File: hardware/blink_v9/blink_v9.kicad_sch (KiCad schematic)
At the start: 117 parts, among them J1 Conn_01x02, J14 Conn_02x16_Odd_Even, J15 Conn_01x01, J16 Conn_01x01, J5 Conn_01x06_Pin, J7 Conn_01x06_Pin, J8 Conn_01x06, J9 USB_C_Receptacle, Q1 S8550, Q2 S8050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

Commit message: start swap usb rx/tx
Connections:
- net LEDMY: now also U4.59 (PB7); no longer U4.43 (PA10)
- net NCOL1: now also U4.58 (PB6); no longer U4.42 (PA9)
- net USB_RX: now also U4.42 (PA9); no longer U4.58 (PB6)
- net USB_TX: now also U4.43 (PA10); no longer U4.59 (PB7)
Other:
- moved on the sheet: R17, R20
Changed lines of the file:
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@@
     (stroke (width 0) (type default))
   )
-  (wire (pts (xy 278.13 55.88) (xy 278.13 59.69))
+  (wire (pts (xy 283.21 43.18) (xy 283.21 46.99))
     (stroke (width 0) (type default))
   )
@@
     (stroke (width 0) (type default))
   )
-  (wire (pts (xy 261.62 55.88) (xy 261.62 59.69))
+  (wire (pts (xy 266.7 43.18) (xy 266.7 46.99))
     (stroke (width 0) (type default))
   )
@@
     (effects (font (size 1.27 1.27)) (justify left bottom))
   )
+  (label "USB_RX" (at 242.57 55.88 0) (fields_autoplaced)
+    (effects (font (size 1.27 1.27)) (justify left bottom))
+  )
   (label "DB3" (at 207.01 50.8 180) (fields_autoplaced)
     (effects (font (size 1.27 1.27)) (justify right bottom))
@@
     (effects (font (size 1.27 1.27)) (justify right bottom))
   )
-  (label "LEDMY" (at 242.57 58.42 0) (fields_autoplaced)
-    (effects (font (size 1.27 1.27)) (justify left bottom))
-  )
   (label "HSE_IN" (at 207.01 43.18 180) (fields_autoplaced)
     (effects (font (size 1.27 1.27)) (justify right bottom))
@@
     (effects (font (size 1.27 1.27)) (justify right bottom))
   )
+  (label "USB_TX" (at 242.57 58.42 0) (fields_autoplaced)
+    (effects (font (size 1.27 1.27)) (justify left bottom))
+  )
   (label "NROW5" (at 365.76 58.42 0) (fields_autoplaced)
     (effects (font (size 1.27 1.27)) (justify left bottom))
@@
     (effects (font (size 1.27 1.27)) (justify left bottom))
   )
-  (label "USB_TX" (at 242.57 93.98 0) (fields_autoplaced)
-    (effects (font (size 1.27 1.27)) (justify left bottom))
-  )
   (label "NCOL7" (at 365.76 48.26 0) (fields_autoplaced)
     (effects (font (size 1.27 1.27)) (justify left bottom))
@@
     (effects (font (size 1.27 1.27)) (justify left bottom))
   )
-  (label "PPS_OUT" (at 261.62 50.8 0) (fields_autoplaced)
+  (label "PPS_OUT" (at 266.7 38.1 0) (fields_autoplaced)
     (effects (font (size 1.27 1.27)) (justify left bottom))
   )
@@
     (effects (font (size 1.27 1.27)) (justify right bottom))
   )
-  (label "PPS_OUT" (at 278.13 50.8 0) (fields_autoplaced)
+  (label "PPS_OUT" (at 283.21 38.1 0) (fields_autoplaced)
     (effects (font (size 1.27 1.27)) (justify left bottom))
   )
@@
     (effects (font (size 1.27 1.27)) (justify left bottom))
   )
-  (label "MON_PPS" (at 261.62 59.69 0) (fields_autoplaced)
+  (label "MON_PPS" (at 266.7 46.99 0) (fields_autoplaced)
     (effects (font (size 1.27 1.27)) (justify left bottom))
   )
-  (label "AUX_MON_PPS" (at 278.13 59.69 0) (fields_autoplaced)
+  (label "AUX_MON_PPS" (at 283.21 46.99 0) (fields_autoplaced)
     (effects (font (size 1.27 1.27)) (justify left bottom))
   )
@@
     (effects (font (size 1.27 1.27)) (justify left bottom))
   )
-  (label "USB_RX" (at 242.57 91.44 0) (fields_autoplaced)
-    (effects (font (size 1.27 1.27)) (justify left bottom))
-  )
   (label "AUD_IN" (at 207.01 55.88 180) (fields_autoplaced)
     (effects (font (size 1.27 1.27)) (justify right bottom))
@@
     (effects (font (size 1.27 1.27)) (justify left bottom))
   )
-  (label "NCOL1" (at 242.57 55.88 0) (fields_autoplaced)
-    (effects (font (size 1.27 1.27)) (justify left bottom))
-  )
   (label "SWDCLK" (at 120.65 85.09 0) (fields_autoplaced)
     (effects (font (size 1.27 1.27)) (justify left bottom))
@@
     (effects (font (size 1.27 1.27)) (justify left bottom))
   )
+  (label "NCOL1" (at 242.57 91.44 0) (fields_autoplaced)
+    (effects (font (size 1.27 1.27)) (justify left bottom))
+  )
   (label "Left" (at 46.99 182.88 0) (fields_autoplaced)
     (effects (font (size 1.27 1.27)) (justify left bottom))
@@
     (effects (font (size 1.27 1.27)) (justify right bottom))
   )
+  (label "LEDMY" (at 242.57 93.98 0) (fields_autoplaced)
+    (effects (font (size 1.27 1.27)) (justify left bottom))
+  )
   (label "LED6" (at 152.4 137.16 0) (fields_autoplaced)
     (effects (font (size 1.27 1.27)) (justify left bottom))
@@
     )
   )
-  (symbol (lib_id "Device:R_Small_US") (at 278.13 53.34 0) (unit 1)
+  (symbol (lib_id "Device:R_Small_US") (at 283.21 40.64 0) (unit 1)
     (in_bom yes) (on_board yes) (dnp no) (fields_autoplaced)
-    (property "Reference" "R20" (at 280.67 52.07 0)
+    (property "Reference" "R20" (at 285.75 39.37 0)
       (effects (font (size 1.27 1.27)) (justify left))
     )
-    (property "Value" "1K0" (at 280.67 54.61 0)
+    (property "Value" "1K0" (at 285.75 41.91 0)
       (effects (font (size 1.27 1.27)) (justify left))
     )
-    (property "Footprint" "Resistor_SMD:R_0603_1608Metric" (at 278.13 53.34 0)
+    (property "Footprint" "Resistor_SMD:R_0603_1608Metric" (at 283.21 40.64 0)
       (effects (font (size 1.27 1.27)) hide)
     )
-    (property "Datasheet" "https://jlcpcb.com/partdetail/Yageo-AC0805FR0751RL/C144556#:~:text=Datasheet-,Download,-Source" (at 278.13 53.34 0)
+    (property "Datasheet" "https://jlcpcb.com/partdetail/Yageo-AC0805FR0751RL/C144556#:~:text=Datasheet-,Download,-Source" (at 283.21 40.64 0)
       (effects (font (size 1.27 1.27)) hide)
     )
-    (property "LCSC" "" (at 278.13 53.34 0)
+    (property "LCSC" "" (at 283.21 40.64 0)
       (effects (font (size 1.27 1.27)) hide)
     )
-    (property "JLCPCB Part #" "C21190" (at 278.13 53.34 0)
+    (property "JLCPCB Part #" "C21190" (at 283.21 40.64 0)
       (effects (font (size 1.27 1.27)) hide)
     )
@@
     )
   )
-  (symbol (lib_id "Device:R_Small_US") (at 261.62 53.34 0) (unit 1)
+  (symbol (lib_id "Device:R_Small_US") (at 266.7 40.64 0) (unit 1)
     (in_bom yes) (on_board yes) (dnp no) (fields_autoplaced)
-    (property "Reference" "R17" (at 264.16 52.07 0)
+    (property "Reference" "R17" (at 269.24 39.37 0)
       (effects (font (size 1.27 1.27)) (justify left))
     )
-    (property "Value" "1K0" (at 264.16 54.61 0)
+    (property "Value" "1K0" (at 269.24 41.91 0)
       (effects (font (size 1.27 1.27)) (justify left))
     )
-    (property "Footprint" "Resistor_SMD:R_0603_1608Metric" (at 261.62 53.34 0)
+    (property "Footprint" "Resistor_SMD:R_0603_1608Metric" (at 266.7 40.64 0)
       (effects (font (size 1.27 1.27)) hide)
     )
-    (property "Datasheet" "https://jlcpcb.com/partdetail/Yageo-AC0805FR0751RL/C144556#:~:text=Datasheet-,Download,-Source" (at 261.62 53.34 0)
+    (property "Datasheet" "https://jlcpcb.com/partdetail/Yageo-AC0805FR0751RL/C144556#:~:text=Datasheet-,Download,-Source" (at 266.7 40.64 0)
       (effects (font (size 1.27 1.27)) hide)
     )
-    (property "LCSC" "" (at 261.62 53.34 0)
+    (property "LCSC" "" (at 266.7 40.64 0)
       (effects (font (size 1.27 1.27)) hide)
     )
-    (property "JLCPCB Part #" "C21190" (at 261.62 53.34 0)
+    (property "JLCPCB Part #" "C21190" (at 266.7 40.64 0)
       (effects (font (size 1.27 1.27)) hide)
     )

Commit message: rename sync_in2 to aux
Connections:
- net SYNC_IN2 renamed AUX_SYNC_IN
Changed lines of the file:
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@@
     (effects (font (size 1.27 1.27)) (justify left bottom))
   )
-  (label "SYNC_IN2" (at 207.01 71.12 180) (fields_autoplaced)
+  (label "AUX_SYNC_IN" (at 207.01 71.12 180) (fields_autoplaced)
     (effects (font (size 1.27 1.27)) (justify right bottom))
   )
@@
     (effects (font (size 1.27 1.27)) (justify right bottom))
   )
-  (global_label "SYNC_IN2" (shape input) (at 287.02 217.17 0) (fields_autoplaced)
+  (global_label "AUX_SYNC_IN" (shape input) (at 287.02 217.17 0) (fields_autoplaced)
     (effects (font (size 1.27 1.27)) (justify left))
     (property "Intersheetrefs" "${INTERSHEET_REFS}" (at 298.9368 217.17 0)

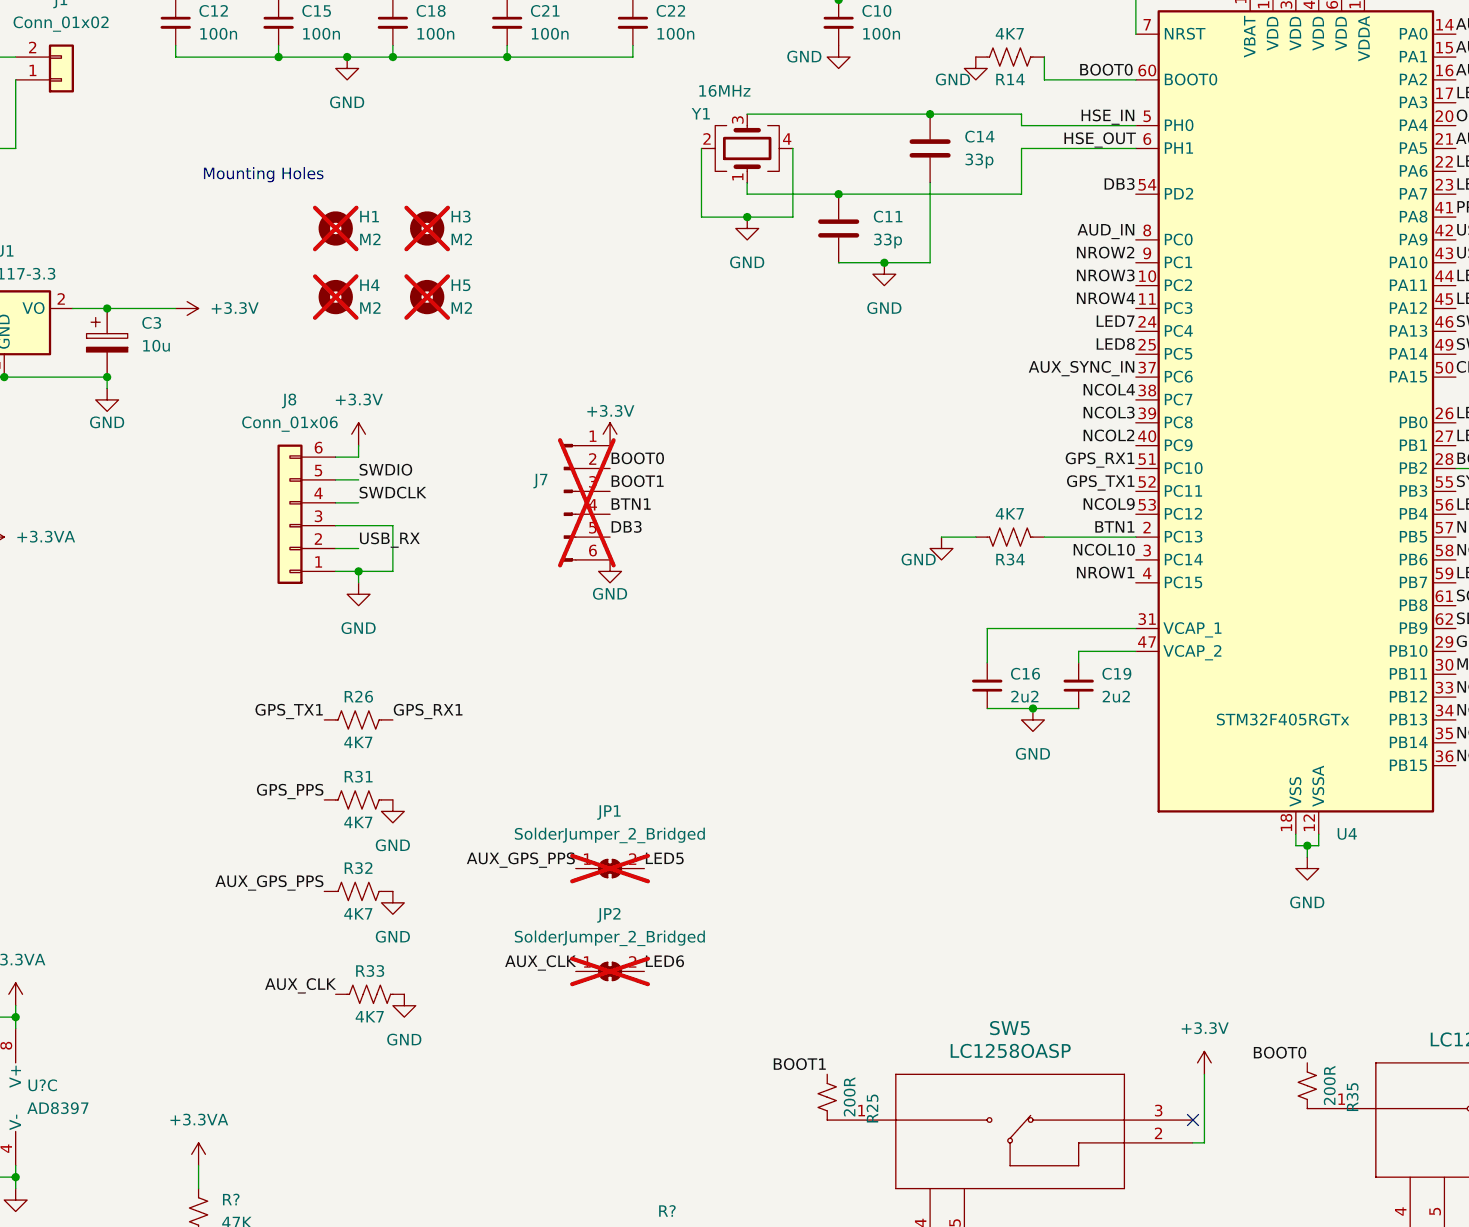
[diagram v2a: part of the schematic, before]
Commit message: update jumpers and swtiches
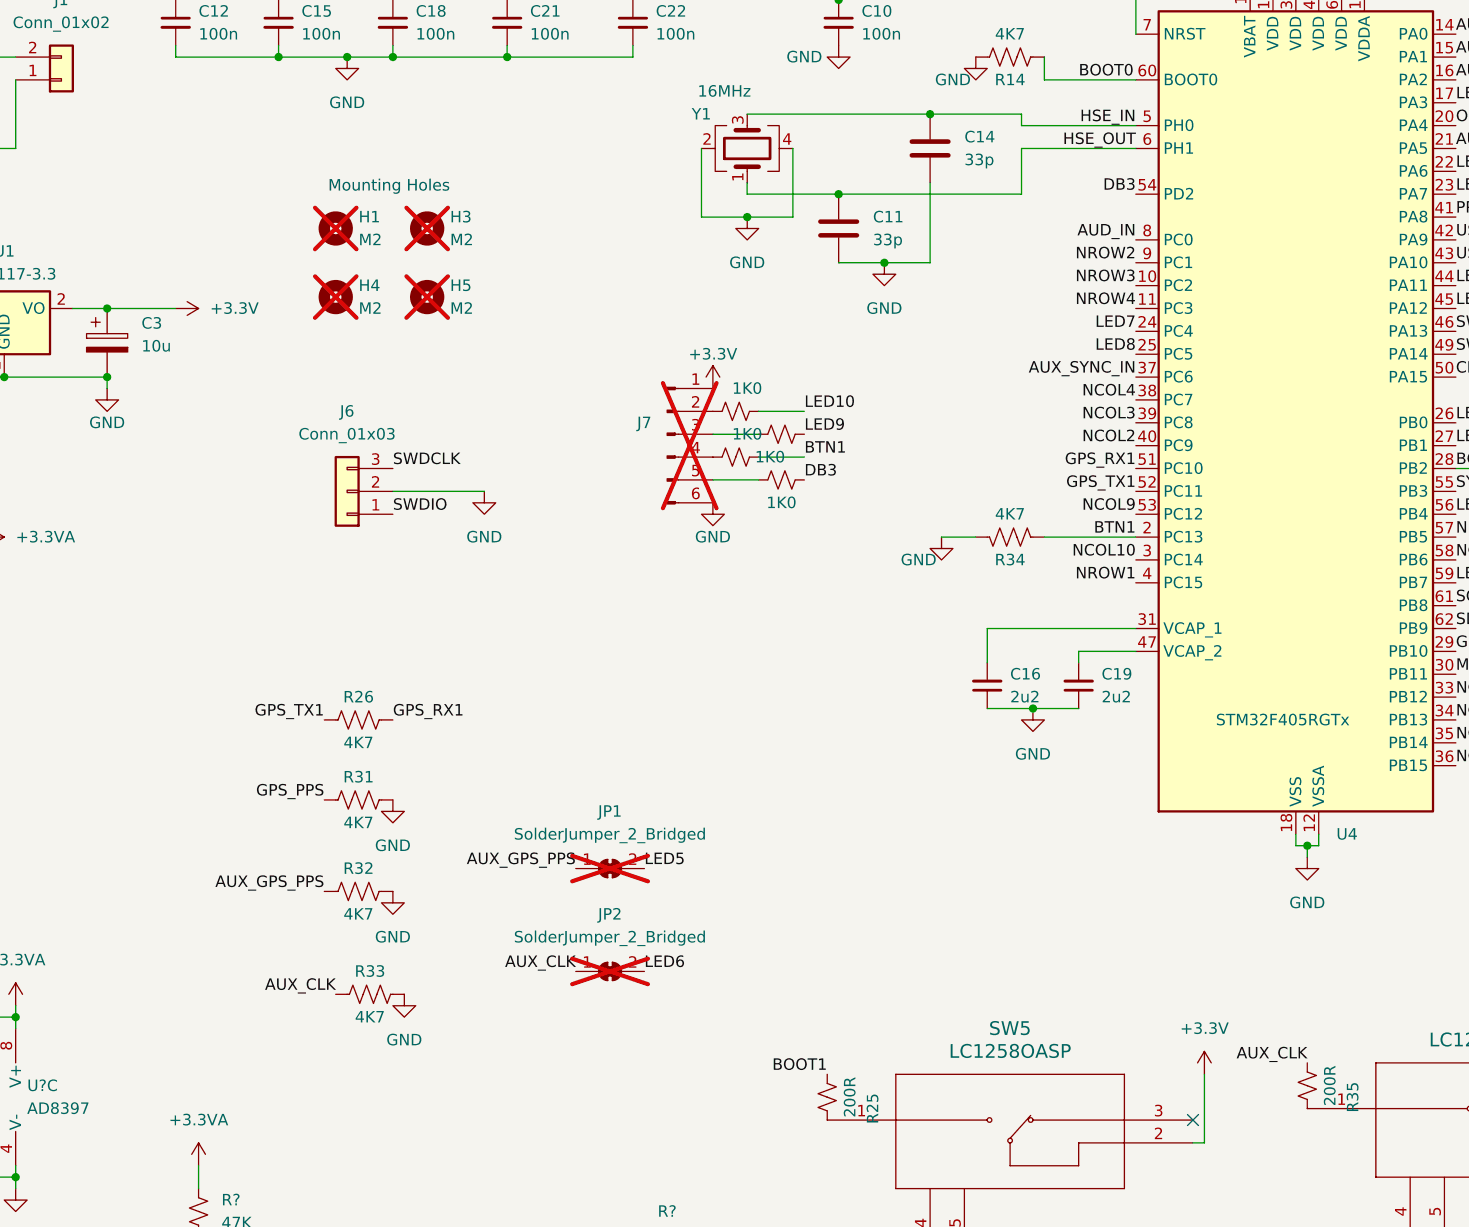
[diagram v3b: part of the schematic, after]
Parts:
- removed J8: Conn_01x06, Connector_JST:JST_PH_S6B-PH-SM4-TB_1x06-1MP_P2.00mm_Horizontal, symbol Connector_Generic:Conn_01x06
- added J6: Conn_01x03, Connector_JST:JST_PH_S3B-PH-SM4-TB_1x03-1MP_P2.00mm_Horizontal, symbol Connector_Generic:Conn_01x03
- added R42, R43, R44, R45: 1K0, Resistor_SMD:R_0603_1608Metric, symbol Device:R_Small_US
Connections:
- net AUX_CLK: now also R35.2
- net BOOT0: no longer J7.2 (Pin_2), R35.2
- net BOOT1: no longer J7.3 (Pin_3)
- net BTN1: now also R44.1; no longer J7.4 (Pin_4)
- net DB3: now also R45.1; no longer J7.5 (Pin_5)
- net GND: now also J6.2 (Pin_2)
- net LED10: now also R42.1
- net LED9: now also R43.1
- net SWDCLK: now also J6.3 (Pin_3)
- net SWDIO: now also J6.1 (Pin_1)
- new net: J7.2 (Pin_2), R42.2
- new net: J7.4 (Pin_4), R44.2
- new net: J7.5 (Pin_5), R45.2
- new net: J7.3 (Pin_3), R43.2
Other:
- moved on the sheet: J7
